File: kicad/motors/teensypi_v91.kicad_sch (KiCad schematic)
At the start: 20 parts, among them M1_center1 MountingHole, M2_center1 MountingHole, M3_center1 MountingHole, M4_center1 MountingHole

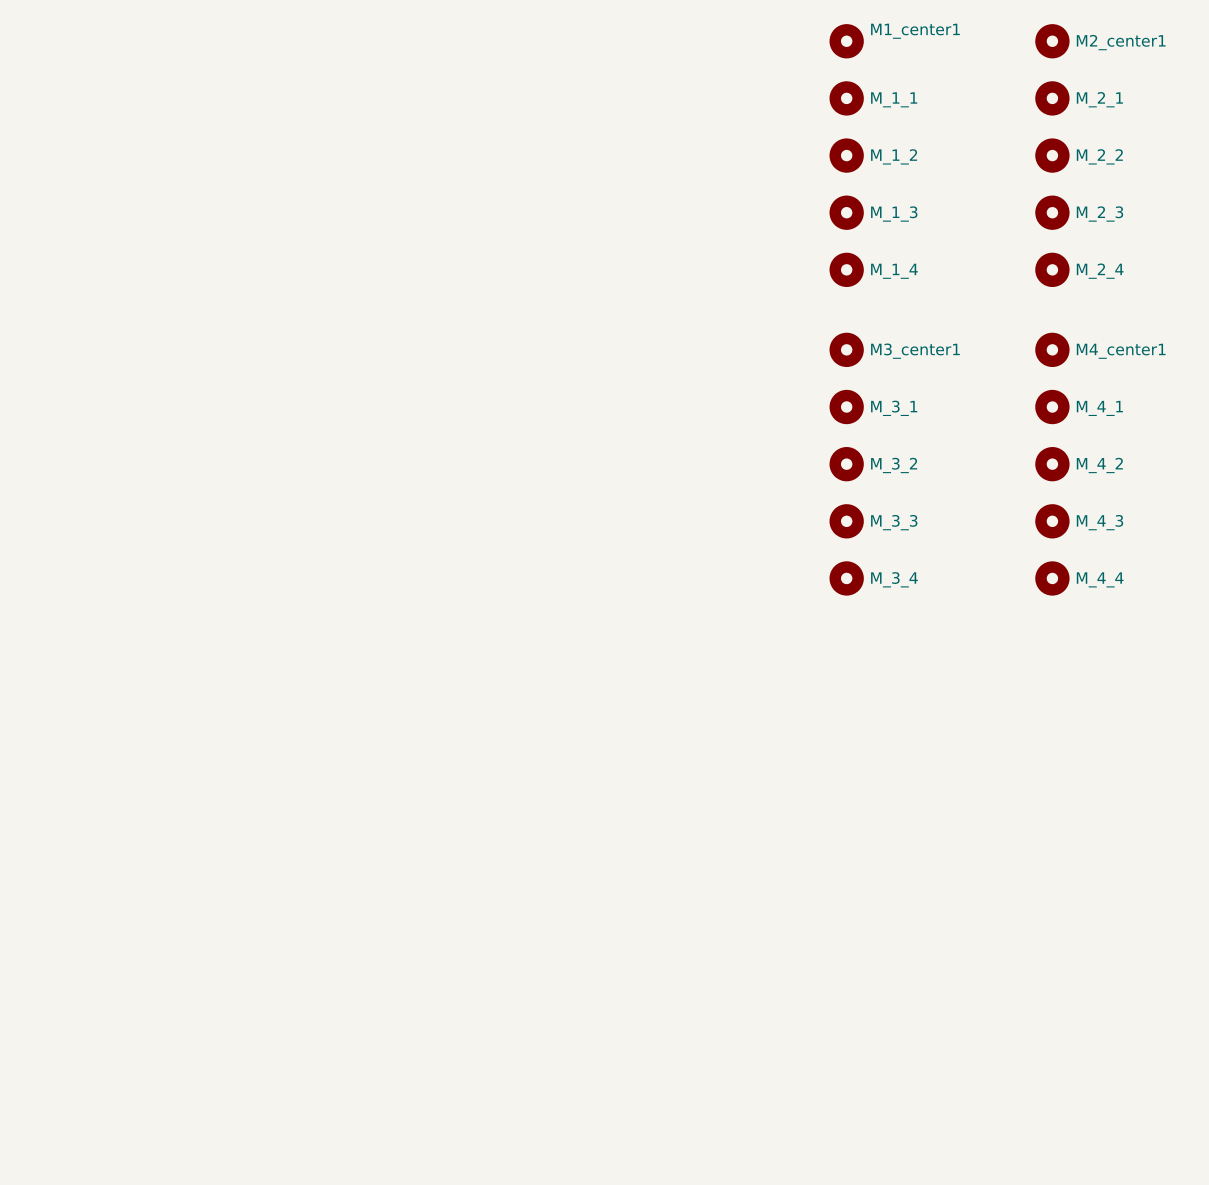
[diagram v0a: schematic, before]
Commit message: modified:   kicad/motors/teensypi_v91.kicad_pcb
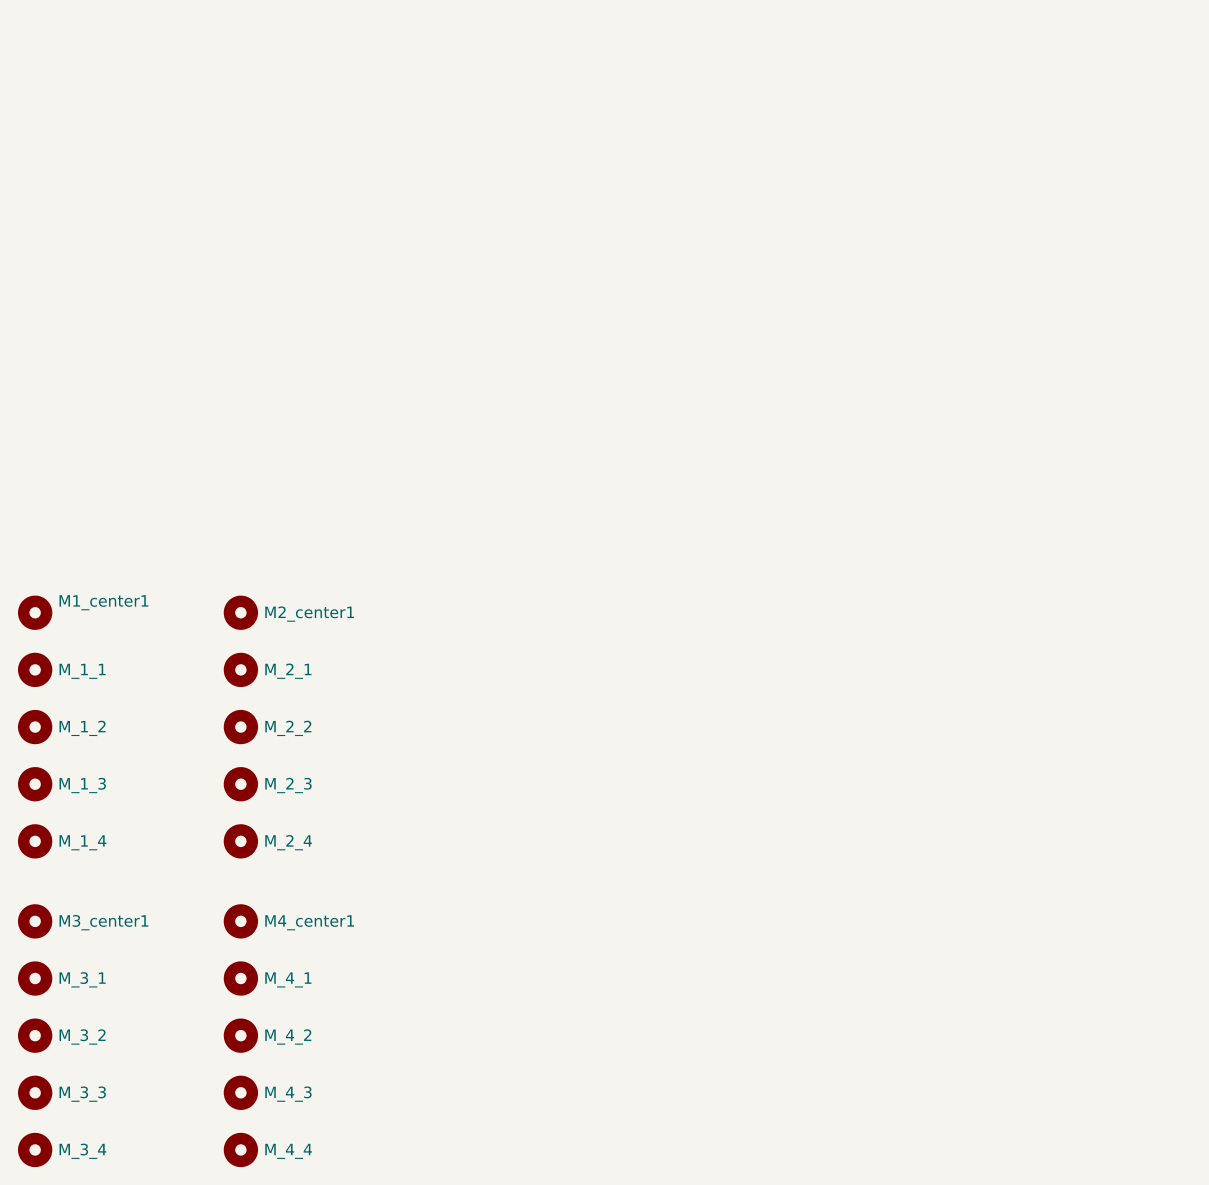
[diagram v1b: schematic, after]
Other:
- moved on the sheet: M1_center1, M2_center1, M3_center1, M4_center1, M_1_1, M_1_2, M_1_3, M_1_4, M_2_1, M_2_2, M_2_3, M_2_4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
